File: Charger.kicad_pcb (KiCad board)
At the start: 2 copper layers, 94.2 x 44.5 mm, 42 parts, among them J1 Input, J2 USB-A-S-X-X-SM2, J3 USB-A-S-X-X-SM2, Q1 BSC42DN25NS3, T1 760875131, U1 LT1085-5.0, U2 TPS2546, U3 LT3798MPMSETRPBF, U4 TPS2546RTER

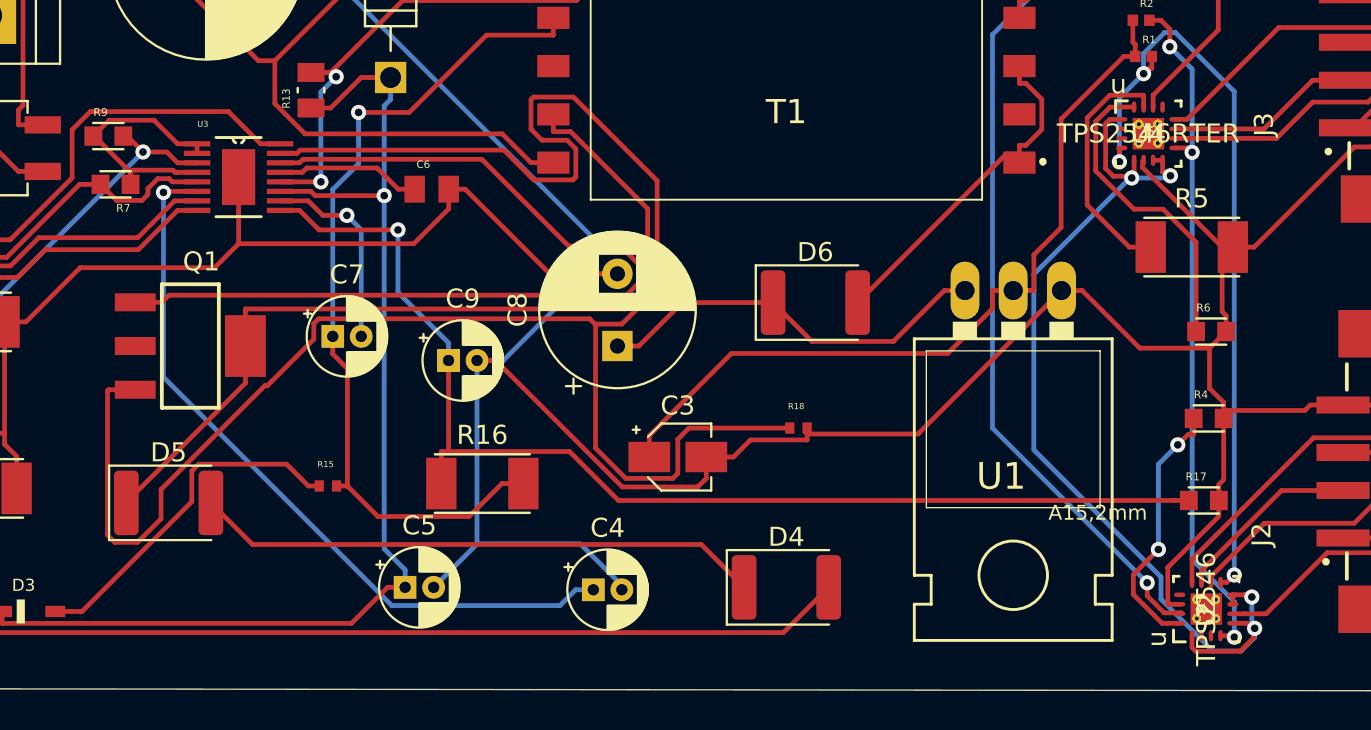
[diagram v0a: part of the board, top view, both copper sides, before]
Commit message: some errors in pcb mitigated
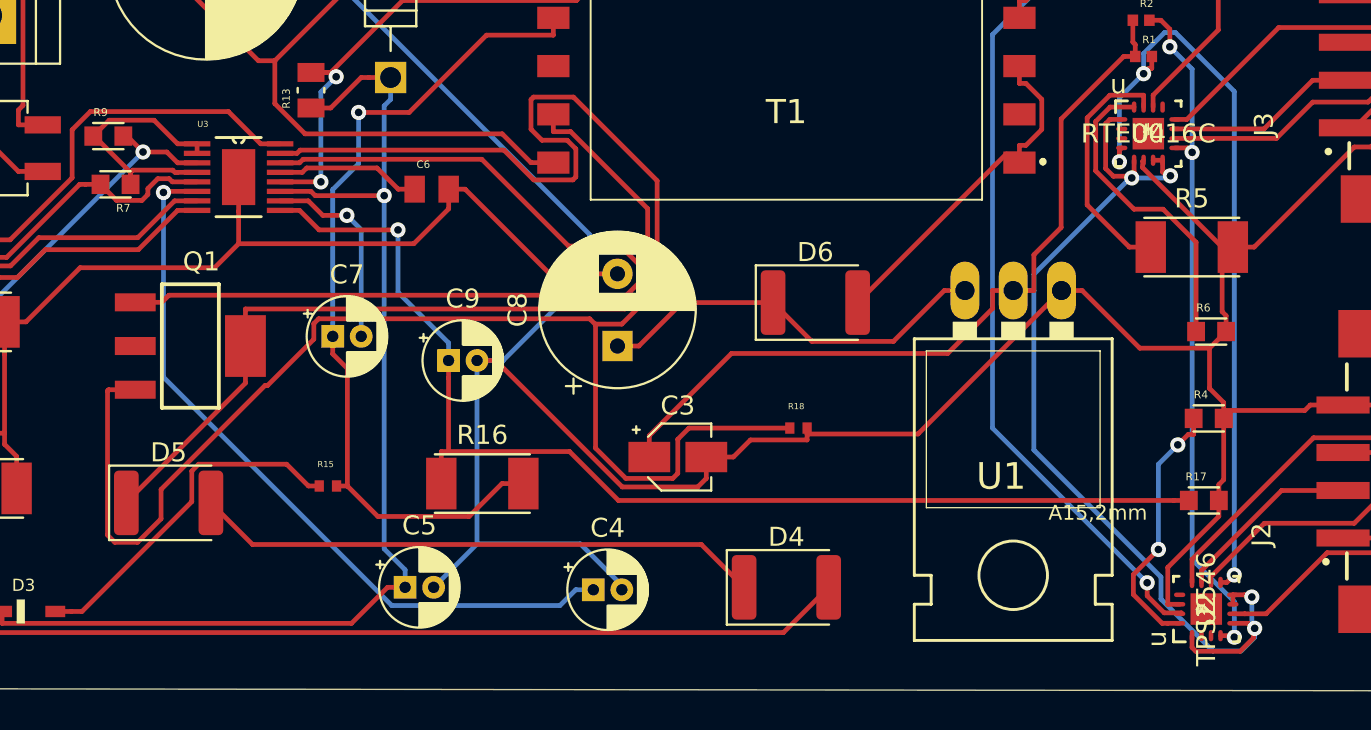
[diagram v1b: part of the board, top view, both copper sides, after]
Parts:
- J2: value USB-A-S-X-X-SM2 -> USB1
- J3: value USB-A-S-X-X-SM2 -> USB2
- U4: value TPS2546RTER -> RTE0016C
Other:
- rule trace_min: 0.2 -> 0.1
- rule via_min_size: 0.4 -> 0.2

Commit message: compact
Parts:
- C2, D4, D5, D6, R1, R10, R11, R12, R13, R14, R15, R16, R17, R18, R2, R3, R4, R6, R8: moved to B.Cu
- moved R10 58.9 mm to (99.3, 43.8)
- moved R11 48.2 mm to (88.6, 38.4)
- moved D3 44.9 mm to (88.4, 53.6)
- moved D5 40.5 mm to (89.5, 45.1)
- moved R16 39.2 mm to (96.3, 34.3)
- moved D1 37.7 mm to (75.2, 68.6)
- moved J1 32.8 mm to (68.2, 62.2)
- moved R9 32.5 mm to (78.6, 62.9)
- moved C2 31.0 mm to (73.2, 62.4)
- moved C7 28.8 mm to (90.6, 64.1)
- moved C5 28.6 mm to (93.7, 60.2)
- moved C9 27.2 mm to (94.1, 67.9)
- moved R8 25.2 mm to (66.7, 45.7)
- moved U3 24.9 mm to (81.4, 56.0)
- moved C6 21.1 mm to (89.0, 51.1)
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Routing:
- net Net-(Q1-Pad3): track 101.2 -> 30.2 mm, vias 0 -> 1
- net gnd: track 300.6 -> 246.2 mm, vias 0 -> 1
- net Net-(R10-Pad1): track 27.5 -> 58.9 mm
- net dcm: track 44.6 -> 74.3 mm
- net Net-(D5-Pad1): track 46.1 -> 18.8 mm, vias 0 -> 1
- net Net-(Q1-Pad1): track 49.2 -> 22.1 mm
- net Net-(C1-Pad1): track 139.0 -> 114.1 mm, vias 0 -> 1
- net Net-(C4-Pad1): track 39.5 -> 16.6 mm
- net Net-(R7-Pad2): track 18.9 -> 41.3 mm, vias 0 -> 1
- net Net-(C8-Pad1): track 21.2 -> 41.7 mm
- net VinL: track 60.5 -> 40.7 mm, vias 1 -> 0
- net Net-(C2-Pad1): track 23.6 -> 9.52 mm, vias 0 -> 1
- net Net-(R7-Pad1): track 13.8 -> 27.2 mm
- net Net-(C2-Pad2): track 20.0 -> 8.55 mm, vias 0 -> 1
- net Stat1: track 41.0 -> 29.6 mm, vias 3 -> 2
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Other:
- board size 94.2 x 44.5 mm -> 71.2 x 43.9 mm

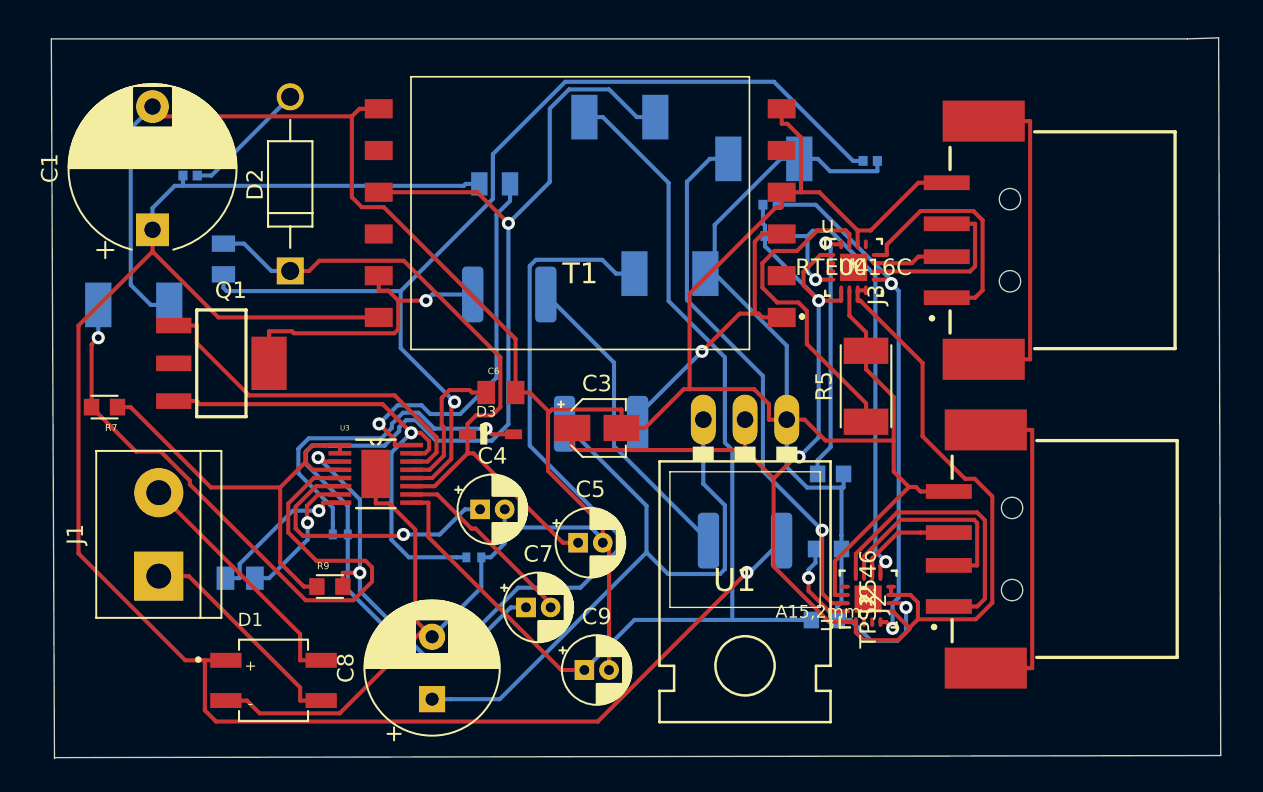
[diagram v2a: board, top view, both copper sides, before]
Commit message: added fuse
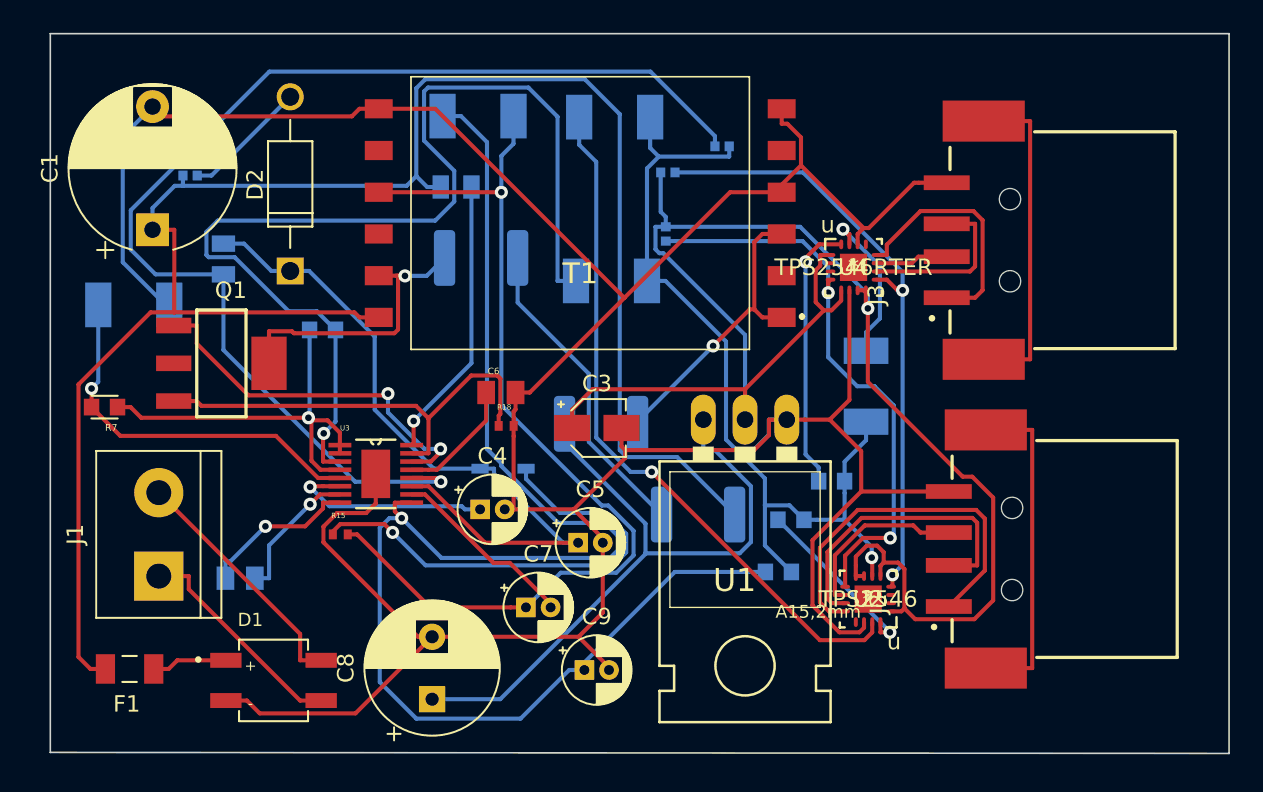
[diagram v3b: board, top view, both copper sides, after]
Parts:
- added F1: 0685T8000-01, fuse:FUSC3215X83N, F.Cu at (66.4, 67.9)
- C1: value 4.7m -> 470u
- D3, R5, R9: moved to B.Cu
- J2: value USB1 -> USB-A-S-X-X-SM2
- J3: value USB2 -> USB-A-S-X-X-SM2
- R15, R18: moved to F.Cu
- U4: value RTE0016C -> TPS2546RTER
- moved R9 15.6 mm to (78.2, 47.2)
- moved R3 9.43 mm to (95.9, 34.3)
- moved R14 9.06 mm to (102.5, 36.1)
- moved R16 8.63 mm to (87.6, 34.2)
- moved R18 8.24 mm to (89.3, 53.1)
- moved R2 6.53 mm to (99.2, 37.7)
- moved R1 6.48 mm to (99.1, 41.4), turned to 270 degrees
- moved R17 4.04 mm to (105.9, 62.0)
- moved R10 3.58 mm to (95.8, 44.3)
- moved D4 3.27 mm to (101.0, 58.5)
- moved R4 2.90 mm to (106.7, 58.8)
- moved D5 2.81 mm to (87.8, 42.9)
- moved R11 2.36 mm to (86.3, 38.5)
- moved D3 2.23 mm to (89.2, 55.7)
- moved R6 0.45 mm to (109.2, 56.5)
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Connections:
- D1 pad 1: Net-(C1-Pad1) -> Net-(D1-Pad1)
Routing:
- net Net-(C9-Pad1): track 66.0 -> 89.2 mm, vias 0 -> 1
- net Net-(R7-Pad2): track 41.3 -> 23.3 mm
- net dcm: track 74.3 -> 58.6 mm
- net gnd: track 246.2 -> 259.5 mm
- net Net-(R5-Pad1): track 19.9 -> 9.83 mm, vias 0 -> 1
- net en: track 63.3 -> 73.0 mm
- net Net-(R3-Pad1): track 33.2 -> 42.7 mm
- net Net-(D3-PadA): track 20.8 -> 28.8 mm
- net Vint: track 91.7 -> 99.2 mm, vias 2 -> 1
- net Vin_sense: track 23.6 -> 17.2 mm
- net Stat1: track 29.6 -> 35.3 mm
- net Net-(R4-Pad1): track 5.47 -> 10.9 mm
- net Stat2: track 32.3 -> 37.7 mm
- net DM1: track 13.4 -> 18.5 mm
- net Net-(R10-Pad1): track 58.9 -> 63.9 mm, vias 2 -> 1
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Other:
- board size 71.2 x 43.9 mm -> 71.8 x 43.8 mm

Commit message: compact
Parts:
- removed J1: Input, TerminalBlock:TerminalBlock_bornier-2_P5.08mm
- added TP1: TestPoint, TestPoint:TestPoint_Pad_2.0x2.0mm, F.Cu at (79.0, 59.4)
- added TP2: TestPoint, TestPoint:TestPoint_Pad_2.0x2.0mm, F.Cu at (78.9, 64.2)
- C1: footprint Capacitor_THT:CP_Radial_D10.0mm_P7.50mm -> Capacitor_SMD:CP_Elec_5x4.4
- C2, R9: moved to F.Cu
- C3: footprint Capacitor_SMD:CP_Elec_3x5.3 -> Capacitor_SMD:CP_Elec_4x3.9
- C4, C5, C7, C9: footprint Capacitor_THT:CP_Radial_D4.0mm_P1.50mm -> Capacitor_SMD:CP_Elec_3x5.3
- C8: footprint Capacitor_THT:CP_Radial_D8.0mm_P3.80mm -> Capacitor_SMD:CP_Elec_5x4.4
- Q1, R15, R7, U3: moved to B.Cu
- moved C1 36.0 mm to (95.7, 63.9), turned to 270 degrees
- moved R7 35.0 mm to (98.2, 41.1), turned to 0 degrees
- moved R13 33.9 mm to (101.2, 60.3)
- moved R10 32.1 mm to (125.3, 56.7), turned to 270 degrees
- moved R8 30.3 mm to (89.0, 66.3)
- moved Q1 28.4 mm to (96.3, 64.1)
- moved D2 24.3 mm to (82.9, 61.7)
- moved R12 22.8 mm to (92.9, 37.4)
- moved R9 22.5 mm to (78.9, 69.7)
- moved F1 19.8 mm to (78.8, 52.5), turned to 90 degrees
- moved R5 19.7 mm to (99.1, 35.1)
- moved D1 18.8 mm to (84.6, 52.3), turned to 180 degrees
- moved U2 18.7 mm to (111.5, 44.9), turned to 0 degrees
- moved C8 18.7 mm to (102.1, 62.7), turned to 270 degrees
- moved D4 17.4 mm to (93.9, 42.7), turned to 90 degrees
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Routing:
- net Net-(C1-Pad1): track 113.6 -> 67.2 mm, vias 0 -> 1
- net Net-(D5-Pad1): track 17.7 -> 52.5 mm
- net Vint: track 99.2 -> 65.0 mm, vias 1 -> 3
- net Net-(R7-Pad1): track 25.2 -> 59.0 mm
- net Stat2: track 37.7 -> 15.7 mm
- net Net-(D2-PadA): track 7.65 -> 29.5 mm
- net Net-(C4-Pad1): track 12.7 -> 33.1 mm
- net en: track 73.0 -> 52.8 mm, vias 1 -> 0
- net Net-(D3-PadA): track 28.8 -> 10.1 mm, vias 1 -> 0
- net Net-(R7-Pad2): track 23.3 -> 41.7 mm, vias 1 -> 0
- net Net-(R3-Pad1): track 42.7 -> 24.4 mm
- net Net-(C8-Pad1): track 42.4 -> 25.4 mm, vias 0 -> 1
- net Net-(C9-Pad1): track 89.2 -> 104.9 mm
- net Stat1: track 35.3 -> 20.4 mm
- net DM2: track 4.44 -> 19.1 mm
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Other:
- board size 71.8 x 43.8 mm -> 57.2 x 42 mm

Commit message: updates
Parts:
- removed C1: 470u, Capacitor_SMD:CP_Elec_5x4.4
- C2, D1, F1, R18, R9, U2, U4: moved to B.Cu
- R12, R14, R15: moved to F.Cu
- moved R5 93.9 mm to (179.0, 84.5)
- moved F1 92.6 mm to (171.4, 50.4), turned to 0 degrees
- moved R16 90.8 mm to (150.5, 97.9)
- moved R8 89.9 mm to (178.8, 64.8), turned to 90 degrees
- moved R1 86.9 mm to (169.3, 95.4), turned to 0 degrees
- moved C7 86.4 mm to (172.2, 96.4), turned to 0 degrees
- moved C2 79.1 mm to (156.2, 74.3)
- moved R4 77.5 mm to (177.9, 89.2)
- moved C5 76.9 mm to (164.0, 51.4)
- moved R11 75.5 mm to (151.4, 74.4), turned to 180 degrees
- moved TP1 75.4 mm to (144.7, 96.5)
- moved T1 73.5 mm to (158.9, 68.8), turned to 270 degrees
- moved U3 72.4 mm to (155.0, 86.4), turned to 0 degrees
- moved TP2 71.6 mm to (144.7, 92.4)
- moved R3 70.5 mm to (156.1, 65.9)
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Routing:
- net VinL: track 46.7 -> 90.8 mm
- net Net-(C9-Pad1): track 104.9 -> 61.6 mm
- net AC1: track 12.5 -> 54.8 mm, vias 0 -> 1
- net Stat1: track 20.4 -> 56.8 mm, vias 2 -> 0
- net AC2: track 18.1 -> 48.3 mm, vias 0 -> 1
- net Net-(R10-Pad1): track 66.2 -> 37.5 mm
- net Net-(D2-PadA): track 29.5 -> 2.52 mm
- net Net-(C6-Pad1): track 8.24 -> 35.2 mm
- net gnd: track 247.5 -> 272.9 mm, vias 1 -> 4
- net dcm: track 45.3 -> 69.5 mm, vias 2 -> 1
- net Net-(C8-Pad1): track 25.4 -> 47.9 mm
- net Net-(R7-Pad2): track 41.7 -> 63.1 mm
- net en: track 52.8 -> 34.9 mm, vias 0 -> 1
- net Net-(R7-Pad1): track 59.0 -> 42.4 mm, vias 1 -> 0
- net Net-(D5-Pad1): track 52.5 -> 36.9 mm, vias 1 -> 2
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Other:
- board size 57.2 x 42 mm -> 41.9 x 56.1 mm

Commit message: updated size
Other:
- board size 41.9 x 56.1 mm -> 42.6 x 59.8 mm
